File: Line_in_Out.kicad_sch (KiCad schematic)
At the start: 0 parts

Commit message: Added oled hierarchical page and referenced other pages
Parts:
- added J?: In Left, ksoloti_shield_footprints:Jack_6.35mm_Neutrik_NRJ6HF_Horizontal_no_screwhole, symbol ksoloti_shield_symbols:AudioJack_6.35mm_TRS_Neutrik_NRJ6HF
- added J?: Out Left, ksoloti_shield_footprints:Jack_6.35mm_Neutrik_NRJ6HF_Horizontal_no_screwhole, symbol ksoloti_shield_symbols:AudioJack_6.35mm_TRS_Neutrik_NRJ6HF
- added J?: Headphones Out, Connector_Audio:Jack_3.5mm_CUI_SJ1-3513N_Horizontal, symbol ksoloti_shield_symbols:AudioJack3_3.5mm_Stereo_SwitchT_WQP729JH-Blue_from_Thonk
- added J?: In Right, ksoloti_shield_footprints:Jack_6.35mm_Neutrik_NRJ6HF_Horizontal_no_screwhole, symbol ksoloti_shield_symbols:AudioJack_6.35mm_TRS_Neutrik_NRJ6HF
- added J?: Out Right, ksoloti_shield_footprints:Jack_6.35mm_Neutrik_NRJ6HF_Horizontal_no_screwhole, symbol ksoloti_shield_symbols:AudioJack_6.35mm_TRS_Neutrik_NRJ6HF
- added RV?: R_POT_Dual_Separate_GND, ksoloti_shield_footprints:ALPS_POT_VERTICAL_PS_DUAL, symbol ksoloti_shield_symbols:R_POT_Dual_Separate_GND
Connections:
- new net HP_GND: J?.S
- new net HP_L: J?.T
- new net HP_R: J?.R
- new net IN_GND: J?.S, J?.S
- new net IN_L: J?.T
- new net IN_R: J?.T
- new net OUT_GND: J?.S, J?.S
- new net OUT_L: J?.T
- new net OUT_R: J?.T
- no-connect marks 0 -> 1
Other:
- note added: "J1: LINE IN/OUT"
- note added: "J2: PHONES OUT"

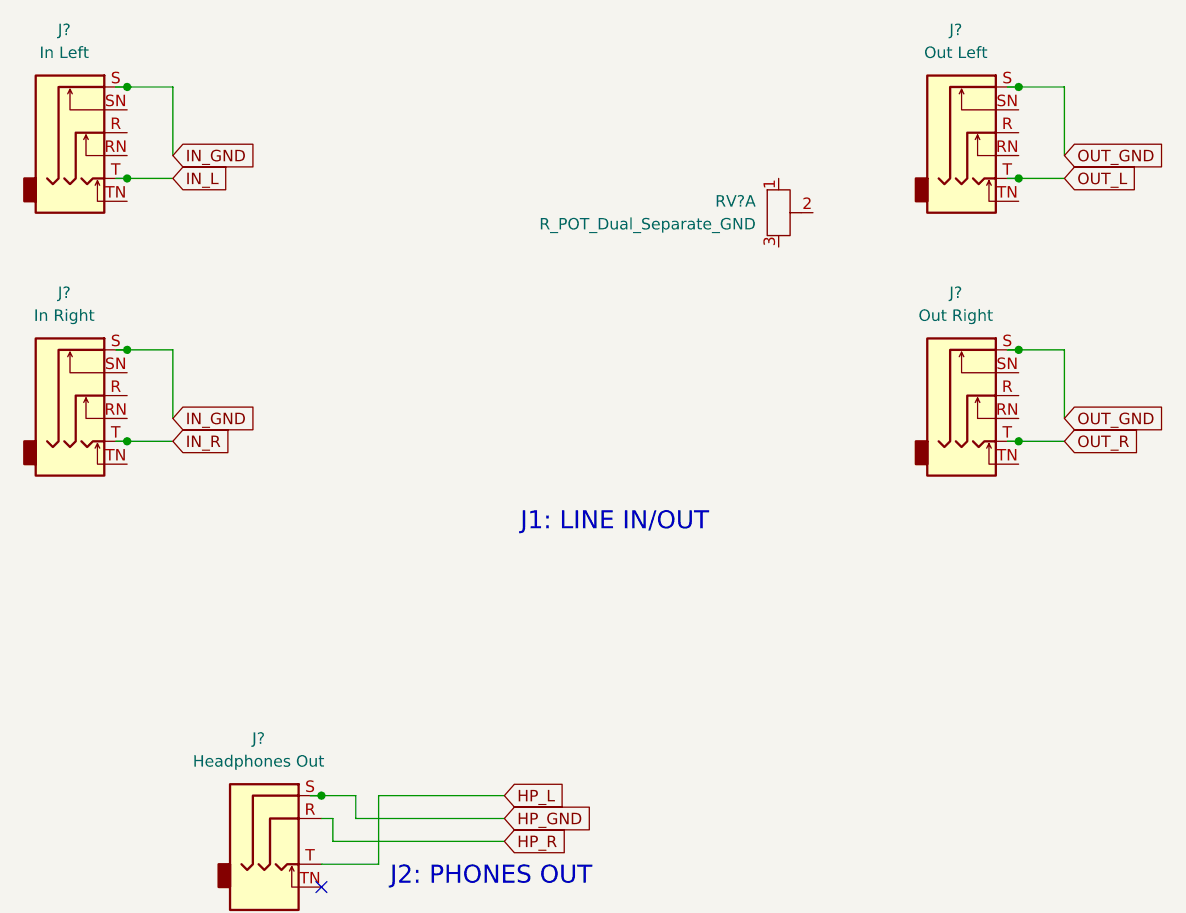
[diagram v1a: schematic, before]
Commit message: Fixed pcb and ran some electrical rule checking and fixed some issues mainly connections and power flags
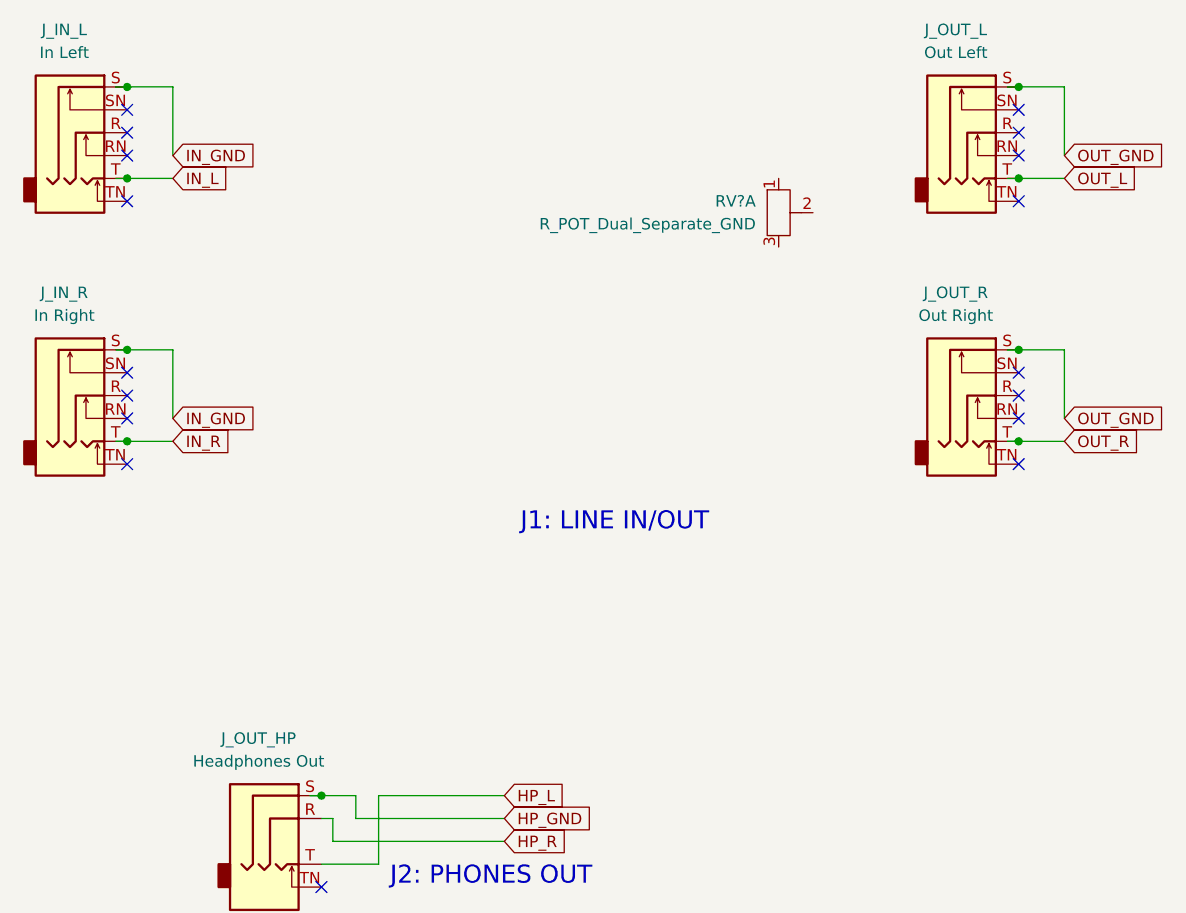
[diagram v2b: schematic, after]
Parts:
- gave numbers to parts that had none: 5
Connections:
- no-connect marks 1 -> 17
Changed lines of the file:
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@@
+	)
+	(no_connect
+		(at 157.48 73.66)
 	)
 	(no_connect
 		(at 80.01 128.27)
+	)
+	(no_connect
+		(at 157.48 46.99)
+	)
+	(no_connect
+		(at 157.48 44.45)
+	)
+	(no_connect
+		(at 58.42 71.12)
+	)
+	(no_connect
+		(at 58.42 41.91)
+	)
+	(no_connect
+		(at 157.48 41.91)
+	)
+	(no_connect
+		(at 157.48 81.28)
+	)
+	(no_connect
+		(at 157.48 71.12)
+	)
+	(no_connect
+		(at 58.42 52.07)
+	)
+	(no_connect
+		(at 58.42 44.45)
+	)
+	(no_connect
+		(at 58.42 73.66)
+	)
+	(no_connect
+		(at 58.42 81.28)
+	)
+	(no_connect
+		(at 157.48 76.2)
+	)
+	(no_connect
+		(at 58.42 76.2)
+	)
+	(no_connect
+		(at 58.42 46.99)
+	)
+	(no_connect
+		(at 157.48 52.07)
 	)
 	(wire
@@
 		(dnp no)
 		(fields_autoplaced yes)
-		(property "Reference" "J?"
+		(property "Reference" "J_IN_L"
 			(at 51.435 33.02 0)
 			(effects
@@
 			(project "diggi_shield_2"
 				(path "/21684161-6457-4723-8fc3-25d7330779e2/2c1ec2b5-4b06-4755-8228-7d0a032d790f"
-					(reference "J?")
+					(reference "J_IN_L")
 					(unit 1)
 				)
@@
 		(dnp no)
 		(fields_autoplaced yes)
-		(property "Reference" "J?"
+		(property "Reference" "J_OUT_L"
 			(at 150.495 33.02 0)
 			(effects
@@
 			(project "diggi_shield_2"
 				(path "/21684161-6457-4723-8fc3-25d7330779e2/2c1ec2b5-4b06-4755-8228-7d0a032d790f"
-					(reference "J?")
+					(reference "J_OUT_L")
 					(unit 1)
 				)
@@
 		(dnp no)
 		(fields_autoplaced yes)
-		(property "Reference" "J?"
+		(property "Reference" "J_OUT_HP"
 			(at 73.025 111.76 0)
 			(effects
@@
 			(project "diggi_shield_2"
 				(path "/21684161-6457-4723-8fc3-25d7330779e2/2c1ec2b5-4b06-4755-8228-7d0a032d790f"
-					(reference "J?")
+					(reference "J_OUT_HP")
 					(unit 1)
 				)
@@
 		(dnp no)
 		(fields_autoplaced yes)
-		(property "Reference" "J?"
+		(property "Reference" "J_IN_R"
 			(at 51.435 62.23 0)
 			(effects
@@
 			(project "diggi_shield_2"
 				(path "/21684161-6457-4723-8fc3-25d7330779e2/2c1ec2b5-4b06-4755-8228-7d0a032d790f"
-					(reference "J?")
+					(reference "J_IN_R")
 					(unit 1)
 				)
@@
 		(dnp no)
 		(fields_autoplaced yes)
-		(property "Reference" "J?"
+		(property "Reference" "J_OUT_R"
 			(at 150.495 62.23 0)
 			(effects
@@
 			(project "diggi_shield_2"
 				(path "/21684161-6457-4723-8fc3-25d7330779e2/2c1ec2b5-4b06-4755-8228-7d0a032d790f"
-					(reference "J?")
+					(reference "J_OUT_R")
 					(unit 1)
 				)

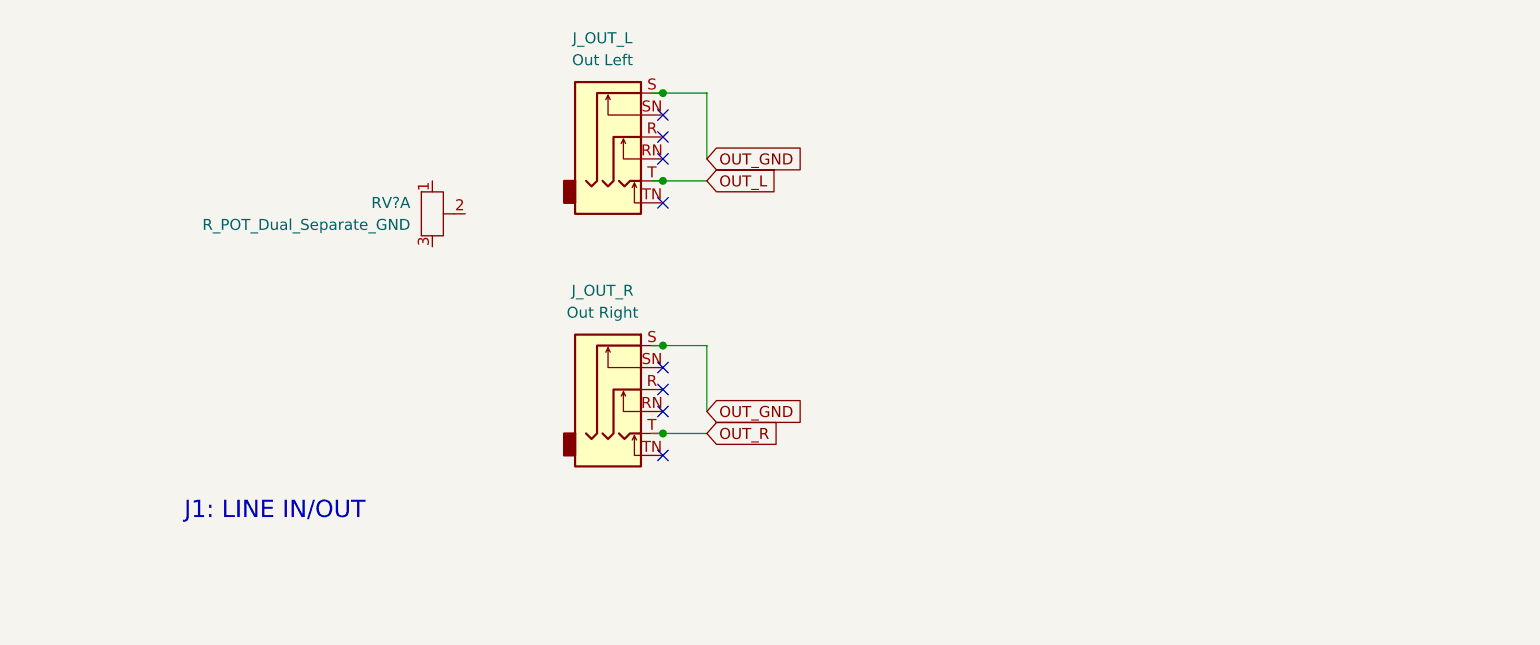
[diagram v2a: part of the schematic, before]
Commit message: Adding line out circuitry based on gills schematic
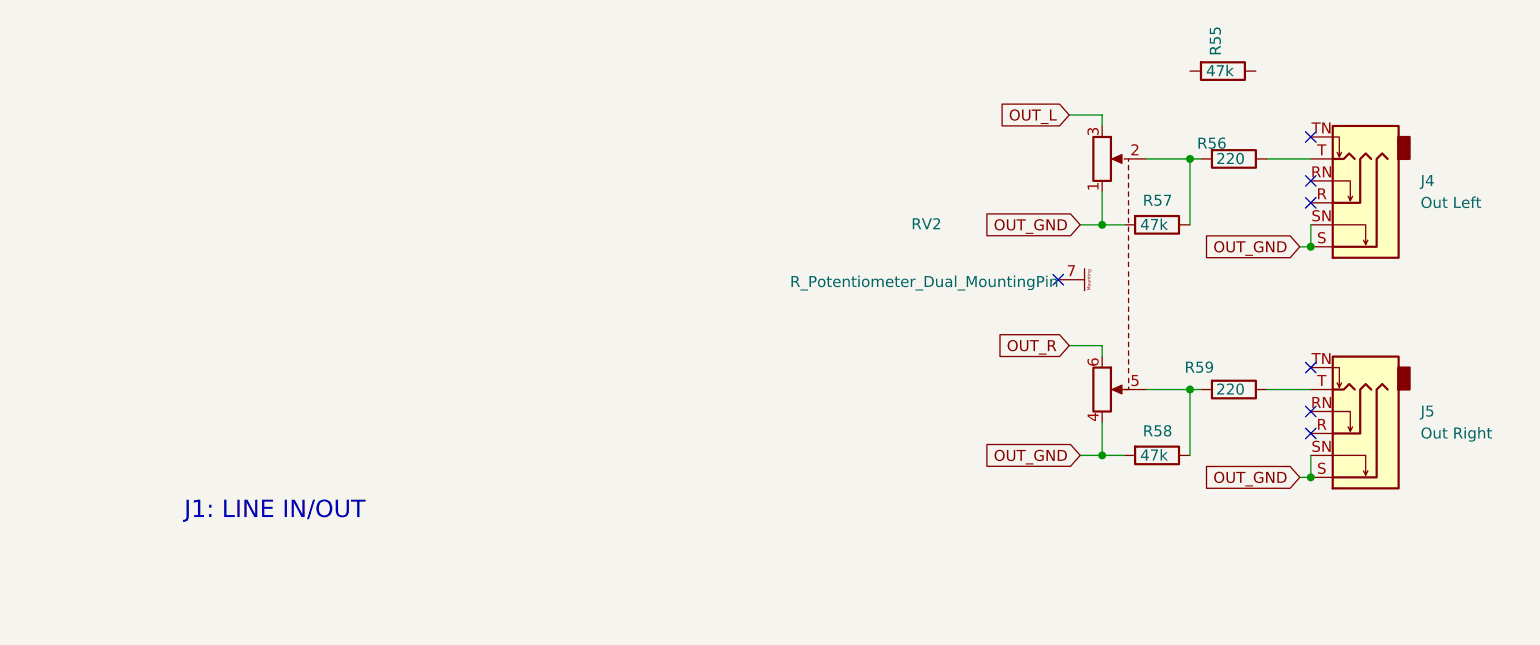
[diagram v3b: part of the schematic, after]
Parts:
- removed RV?: R_POT_Dual_Separate_GND, ksoloti_shield_footprints:ALPS_POT_VERTICAL_PS_DUAL, symbol ksoloti_shield_symbols:R_POT_Dual_Separate_GND
- added R55, R57, R58: 47k, Resistor_SMD:R_0603_1608Metric, symbol Device:R
- added R56, R59: 220, Resistor_SMD:R_0603_1608Metric, symbol Device:R
- added RV2: R_Potentiometer_Dual_MountingPin, ksoloti_shield_footprints:ALPS_POT_VERTICAL_PS_DUAL, symbol Device:R_Potentiometer_Dual_MountingPin
- renumbered J_OUT_L to J4, J_OUT_R to J5
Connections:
- net OUT_GND: now also J4.SN, J5.SN, R57.2, R58.2, RV2.1, RV2.4
- net OUT_L: now also RV2.3; no longer J4.T
- net OUT_R: now also RV2.6; no longer J5.T
- new net: J5.T, R59.1
- new net: R58.1, R59.2, RV2.5
- new net: R56.2, R57.1, RV2.2
- new net: J4.T, R56.1
- no-connect marks 17 -> 16
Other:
- moved on the sheet: J4, J5

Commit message: Annotated all components (numerating)
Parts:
- renumbered J_IN_L to J_IN_L1, J_IN_R to J_IN_R1, J_OUT_HP to J_OUT_HP1
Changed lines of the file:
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@@
 		(dnp no)
 		(fields_autoplaced yes)
-		(property "Reference" "J_IN_L"
+		(property "Reference" "J_IN_L1"
 			(at 51.435 33.02 0)
 			(effects
@@
 			(project "diggi_shield_2"
 				(path "/21684161-6457-4723-8fc3-25d7330779e2/2c1ec2b5-4b06-4755-8228-7d0a032d790f"
-					(reference "J_IN_L")
+					(reference "J_IN_L1")
 					(unit 1)
 				)
@@
 		(dnp no)
 		(fields_autoplaced yes)
-		(property "Reference" "J_OUT_HP"
+		(property "Reference" "J_OUT_HP1"
 			(at 73.025 111.76 0)
 			(effects
@@
 			(project "diggi_shield_2"
 				(path "/21684161-6457-4723-8fc3-25d7330779e2/2c1ec2b5-4b06-4755-8228-7d0a032d790f"
-					(reference "J_OUT_HP")
+					(reference "J_OUT_HP1")
 					(unit 1)
 				)
@@
 		(dnp no)
 		(fields_autoplaced yes)
-		(property "Reference" "J_IN_R"
+		(property "Reference" "J_IN_R1"
 			(at 51.435 62.23 0)
 			(effects
@@
 			(project "diggi_shield_2"
 				(path "/21684161-6457-4723-8fc3-25d7330779e2/2c1ec2b5-4b06-4755-8228-7d0a032d790f"
-					(reference "J_IN_R")
-					(unit 1)
-				)
+					(reference "J_IN_R1")
+					(unit 1)
+				)

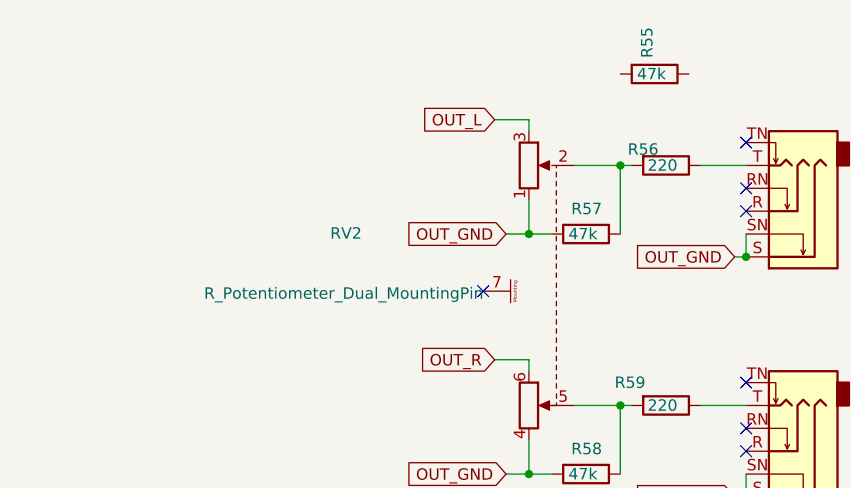
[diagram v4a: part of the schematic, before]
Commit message: Cleaned up ERC errors
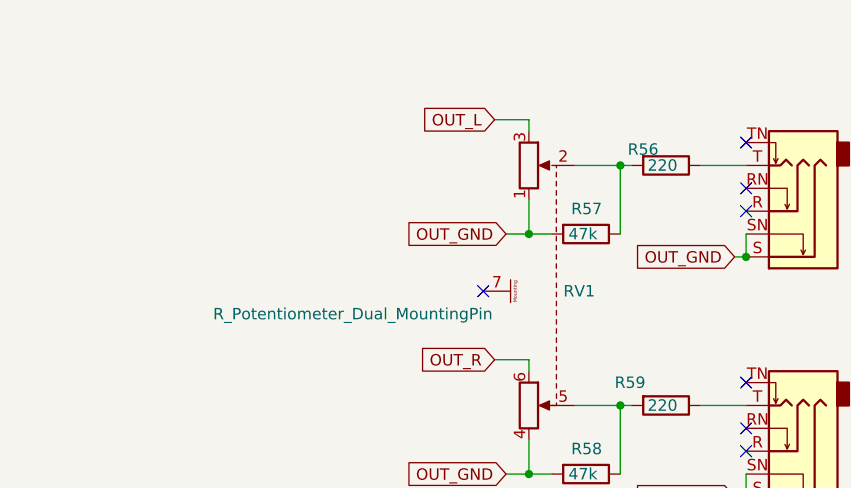
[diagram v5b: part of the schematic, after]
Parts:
- removed R55: 47k, Resistor_SMD:R_0603_1608Metric, symbol Device:R
- renumbered RV2 to RV1
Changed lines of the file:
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@@
 		(on_board yes)
 		(dnp no)
-		(property "Reference" "RV2"
-			(at 187.96 54.5398 90)
+		(property "Reference" "RV1"
+			(at 213.868 60.96 90)
 			(effects
 				(font
@@
 		)
 		(property "Value" "R_Potentiometer_Dual_MountingPin"
-			(at 187.706 61.214 90)
+			(at 188.722 63.5 90)
 			(effects
 				(font
@@
 			(project "diggi_shield_2"
 				(path "/21684161-6457-4723-8fc3-25d7330779e2/2c1ec2b5-4b06-4755-8228-7d0a032d790f"
-					(reference "RV2")
+					(reference "RV1")
 					(unit 1)
 				)
@@
 					(unit 1)
 				)
-			)
-		)
-	)
-	(symbol
-		(lib_id "Device:R")
-		(at 222.25 36.83 270)
-		(unit 1)
-		(exclude_from_sim no)
-		(in_bom yes)
-		(on_board yes)
-		(dnp no)
-		(property "Reference" "R55"
-			(at 221.4153 35.052 0)
-			(effects
-				(font
-					(size 1.27 1.27)
-				)
-				(justify right)
-			)
-		)
-		(property "Value" "47k"
-			(at 223.52 36.83 90)
-			(effects
-				(font
-					(size 1.27 1.27)
-				)
-				(justify right)
-			)
-		)
-		(property "Footprint" "Resistor_SMD:R_0603_1608Metric"
-			(at 222.25 35.052 90)
-			(effects
-				(font
-					(size 1.27 1.27)
-				)
-				(hide yes)
-			)
-		)
-		(property "Datasheet" "~"
-			(at 222.25 36.83 0)
-			(effects
-				(font
-					(size 1.27 1.27)
-				)
-				(hide yes)
-			)
-		)
-		(property "Description" ""
-			(at 222.25 36.83 0)
-			(effects
-				(font
-					(size 1.27 1.27)
-				)
-				(hide yes)
-			)
-		)
-		(pin "1"
-		)
-		(pin "2"
-		)
-		(instances
-			(project "diggi_shield_2"
-				(path "/21684161-6457-4723-8fc3-25d7330779e2/2c1ec2b5-4b06-4755-8228-7d0a032d790f"
-					(reference "R55")
-					(unit 1)
-				)

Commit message: Removed final warnings
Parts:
- RV1: symbol Device:R_Potentiometer_Dual_MountingPin -> diggi:R_Potentiometer_Dual_MountingPin_Diggi
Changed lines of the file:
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@@
 	)
 	(symbol
-		(lib_id "Device:R_Potentiometer_Dual_MountingPin")
+		(lib_id "diggi:R_Potentiometer_Dual_MountingPin_Diggi")
 		(at 210.82 60.96 270)
 		(unit 1)
